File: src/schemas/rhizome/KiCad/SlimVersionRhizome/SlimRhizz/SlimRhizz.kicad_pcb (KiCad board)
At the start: 4 copper layers, 136 x 34.5 mm, 19 parts, among them J1 POWER_IN, J2 WS2812_Tip1, J3 WS2812_Tip2, J4 APA102_Strip, J5 Haptic_DRV1, J6 Haptic_DRV2, J7 Pogo_Male, J8 Pogo_Female, U2 74AHCT125

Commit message: Update PCB
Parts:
- added G***: LOGO, Logo Synapse:logo, B.Cu at (119.5, 124.0)
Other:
- board text added: "+"
- board text added: "-"
- board text added: "Haptic_Femelle"
- board text added: "Haptic_Male"
- board text added: "LED_Embout_Femelle"
- board text added: "LED_Embout_Male"
- board text added: "Power_in"
- board text added: "Serial_Male"

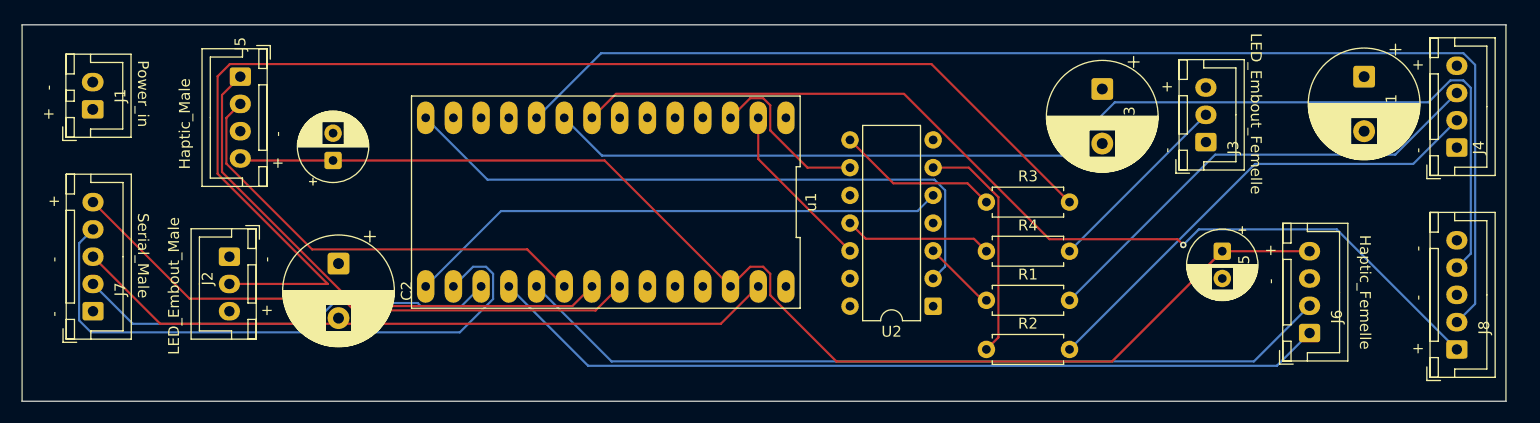
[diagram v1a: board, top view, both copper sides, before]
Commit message: Update PCB SlimRhizz
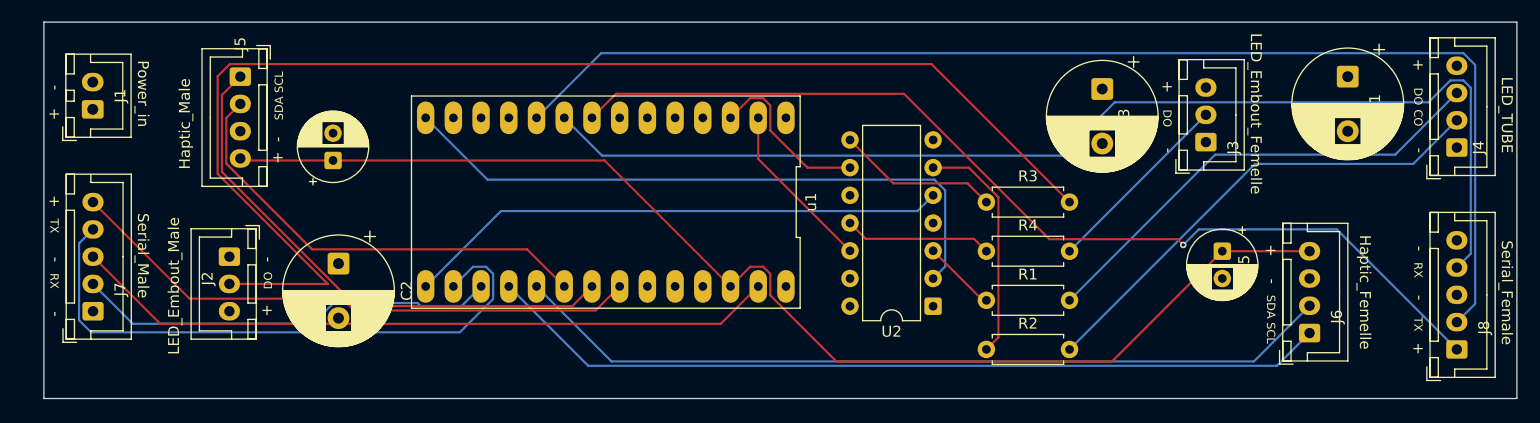
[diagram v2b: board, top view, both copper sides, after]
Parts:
- J4: value APA102_Strip -> LED_TUBE
- moved C1 1.50 mm to (177.0, 112.0)
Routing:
- net GND: track 71.2 -> 71.8 mm
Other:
- board size 136 x 34.5 mm -> 135 x 34.5 mm
- board text added: "CO"
- board text added: "DO"
- board text added: "LED_TUBE"
- board text added: "RX"
- board text added: "SCL"
- board text added: "SDA"
- board text added: "Serial_Female"
- board text added: "TX"
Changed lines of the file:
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@@
 			)
 		)
-		(property "Value" "APA102_Strip"
-			(at 3.75 4.6 90)
+		(property "Value" "LED_TUBE"
+			(at -3.5 -0.5 90)
 			(layer "F.Fab")
+			(hide yes)
 			(effects
 				(font
@@
 	(footprint "Capacitor_THT:CP_Radial_D10.0mm_P5.00mm"
 		(layer "F.Cu")
-		(at 178.5 112 -90)
+		(at 177 112 -90)
 		(descr "CP, Radial series, Radial, pin pitch=5.00mm, diameter=10mm, height=16mm, Electrolytic Capacitor")
 		(tags "CP Radial series Radial pin pitch 5.00mm diameter 10mm height 16mm Electrolytic Capacitor")
@@
 		(tags "CP Radial series Radial pin pitch 5.00mm diameter 10mm height 16mm Electrolytic Capacitor")
 		(property "Reference" "C3"
-			(at 2.5 -2.5 90)
+			(at 2.7 -2.002438 90)
 			(layer "F.SilkS")
 			(effects
@@
 		)
 		(fp_text user "${REFERENCE}"
-			(at 2.5 0 90)
+			(at 2.714285 -2.002438 90)
 			(layer "F.Fab")
 			(effects
@@
 			(at 5 4.6 90)
 			(layer "F.Fab")
+			(hide yes)
 			(effects
 				(font
@@
 			(at 0 0 0)
 			(layer "B.SilkS")
+			(hide yes)
 			(effects
 				(font
@@
 	)
 	(gr_rect
-		(start 55.5 107.25)
-		(end 191.5 141.75)
+		(start 57.5 107)
+		(end 192.5 141.5)
 		(stroke
 			(width 0.05)
@@
 		)
 	)
+	(gr_text "RX"
+		(at 58 130 270)
+		(layer "F.SilkS")
+		(effects
+			(font
+				(size 0.762 0.762)
+				(thickness 0.09525)
+			)
+			(justify left bottom)
+		)
+	)
 	(gr_text "LED_Embout_Male"
 		(at 70 137.5 90)
@@
 		)
 	)
+	(gr_text "SDA"
+		(at 79.5 116 90)
+		(layer "F.SilkS")
+		(effects
+			(font
+				(size 0.762 0.762)
+				(thickness 0.09525)
+			)
+			(justify left bottom)
+		)
+	)
 	(gr_text "Power_in"
 		(at 66 110.5 270)
@@
 	)
 	(gr_text "-"
-		(at 58.5 113.25 90)
+		(at 59 113.25 90)
 		(layer "F.SilkS")
 		(effects
@@
 		)
 	)
+	(gr_text "TX\n"
+		(at 58 125 270)
+		(layer "F.SilkS")
+		(effects
+			(font
+				(size 0.762 0.762)
+				(thickness 0.09525)
+			)
+			(justify left bottom)
+		)
+	)
 	(gr_text "-"
 		(at 184 128 90)
@@
 		)
 	)
+	(gr_text "Serial_Female"
+		(at 191 127 270)
+		(layer "F.SilkS")
+		(effects
+			(font
+				(size 1 1)
+				(thickness 0.1)
+			)
+			(justify left bottom)
+		)
+	)
+	(gr_text "SDA"
+		(at 169.5 132 270)
+		(layer "F.SilkS")
+		(effects
+			(font
+				(size 0.762 0.762)
+				(thickness 0.09525)
+			)
+			(justify left bottom)
+		)
+	)
 	(gr_text "+"
 		(at 161 113.5 90)
@@
 		)
 	)
+	(gr_text "SCL"
+		(at 169.5 134.5 270)
+		(layer "F.SilkS")
+		(effects
+			(font
+				(size 0.762 0.762)
+				(thickness 0.09525)
+			)
+			(justify left bottom)
+		)
+	)
 	(gr_text "+"
 		(at 184 111.5 90)
@@
 		)
 	)
+	(gr_text "DO"
+		(at 78.5 131.5 90)
+		(layer "F.SilkS")
+		(effects
+			(font
+				(size 0.762 0.762)
+				(thickness 0.09525)
+			)
+			(justify left bottom)
+		)
+	)
 	(gr_text "-"
 		(at 161 119 90)
@@
 	)
 	(gr_text "+"
-		(at 79.5 120.5 90)
+		(at 79.5 120 90)
 		(layer "F.SilkS")
 		(effects
@@
 		)
 	)
+	(gr_text "CO"
+		(at 183 115 270)
+		(layer "F.SilkS")
+		(effects
+			(font
+				(size 0.762 0.762)
+				(thickness 0.09525)
+			)
+			(justify left bottom)
+		)
+	)
 	(gr_text "+"
-		(at 58.5 116 90)
+		(at 59 116 90)
 		(layer "F.SilkS")
 		(effects
@@
 		)
 	)
+	(gr_text "DO"
+		(at 160 115 270)
+		(layer "F.SilkS")
+		(effects
+			(font
+				(size 0.762 0.762)
+				(thickness 0.09525)
+			)
+			(justify left bottom)
+		)
+	)
 	(gr_text "-"
 		(at 184 132.5 90)
@@
 		)
 	)
+	(gr_text "RX"
+		(at 183 129 270)
+		(layer "F.SilkS")
+		(effects
+			(font
+				(size 0.762 0.762)
+				(thickness 0.09525)
+			)
+			(justify left bottom)
+		)
+	)
 	(gr_text "+"
 		(at 59 124 90)
@@
 	)
 	(gr_text "-"
-		(at 79.5 117.5 90)
+		(at 79.5 118 90)
 		(layer "F.SilkS")
 		(effects
@@
 		)
 	)
+	(gr_text "LED_TUBE"
+		(at 191 112 270)
+		(layer "F.SilkS")
+		(effects
+			(font
+				(size 1 1)
+				(thickness 0.1)
+			)
+			(justify left bottom)
+		)
+	)
 	(gr_text "Haptic_Male"
 		(at 71 120.5 90)
@@
 		)
 	)
+	(gr_text "SCL"
+		(at 79.5 113.5 90)
+		(layer "F.SilkS")
+		(effects
+			(font
+				(size 0.762 0.762)
+				(thickness 0.09525)
+			)
+			(justify left bottom)
+		)
+	)
 	(gr_text "LED_Embout_Femelle"
 		(at 168 108 270)
@@
 		)
 	)
+	(gr_text "DO"
+		(at 183 113 270)
+		(layer "F.SilkS")
+		(effects
+			(font
+				(size 0.762 0.762)
+				(thickness 0.09525)
+			)
+			(justify left bottom)
+		)
+	)
+	(gr_text "TX\n"
+		(at 183 134 270)
+		(layer "F.SilkS")
+		(effects
+			(font
+				(size 0.762 0.762)
+				(thickness 0.09525)
+			)
+			(justify left bottom)
+		)
+	)
 	(gr_text "-"
 		(at 59 129 90)
@@
 	)
 	(segment
-		(start 177.5 118)
-		(end 178.5 117)
-		(width 0.2)
-		(layer "In1.Cu")
-		(net 34)
-	)
-	(segment
 		(start 131.38 130.5)
 		(end 132.481 129.399)
@@
 	)
 	(segment
+		(start 178.5 118)
+		(end 178.5 117)
+		(width 0.2)
+		(layer "In1.Cu")
+		(net 34)
+	)
+	(segment
 		(start 131.38 130.5)
 		(end 132 130.5)
 		(width 0.2)
 		(layer "In1.Cu")
+		(net 34)
+	)
+	(segment
+		(start 177.5 118)
+		(end 178.5 118)
+		(width 0.2)
+		(layer "In1.Cu")

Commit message: update PCB
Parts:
- moved C4 1.00 mm to (83.0, 119.7)
- moved C1 0.50 mm to (177.5, 112.0)
- moved C2 0.50 mm to (84.0, 129.1)
- moved C5 0.50 mm to (166.0, 128.0)
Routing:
- net +5V: track 425.1 -> 2.82 mm
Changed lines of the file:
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@@
 			(psnegative no)
 			(psa4output no)
-			(plot_black_and_white yes)
+			(plot_black_and_white no)
 			(sketchpadsonfab no)
 			(plotpadnumbers no)
@@
 			(crossoutdnponfab yes)
 			(subtractmaskfromsilk no)
-			(outputformat 1)
+			(outputformat 4)
 			(mirror no)
 			(drillshape 0)
 			(scaleselection 1)
-			(outputdirectory "C:/Users/lepit/Downloads/")
+			(outputdirectory "./")
 		)
 	)
@@
 			(at 0 2 90)
 			(layer "F.SilkS")
+			(hide yes)
 			(effects
 				(font
@@
 	(footprint "Capacitor_THT:CP_Radial_D10.0mm_P5.00mm"
 		(layer "F.Cu")
-		(at 177 112 -90)
+		(at 177.5 112 -90)
 		(descr "CP, Radial series, Radial, pin pitch=5.00mm, diameter=10mm, height=16mm, Electrolytic Capacitor")
 		(tags "CP Radial series Radial pin pitch 5.00mm diameter 10mm height 16mm Electrolytic Capacitor")
 		(property "Reference" "C1"
-			(at 2.5 -2.5 90)
+			(at 2 6 90)
 			(layer "F.SilkS")
 			(effects
@@
 	(footprint "Capacitor_THT:CP_Radial_D6.3mm_P2.50mm"
 		(layer "F.Cu")
-		(at 165.5 128 -90)
+		(at 166 128 -90)
 		(descr "CP, Radial series, Radial, pin pitch=2.50mm, diameter=6.3mm, height=7mm, Electrolytic Capacitor")
 		(tags "CP Radial series Radial pin pitch 2.50mm diameter 6.3mm height 7mm Electrolytic Capacitor")
 		(property "Reference" "C5"
-			(at 1.25 -2 90)
+			(at 1.5 4.5 90)
 			(layer "F.SilkS")
 			(effects
@@
 		(tags "CP Radial series Radial pin pitch 5.00mm diameter 10mm height 16mm Electrolytic Capacitor")
 		(property "Reference" "C3"
-			(at 2.7 -2.002438 90)
+			(at 1.867677 6 90)
 			(layer "F.SilkS")
 			(effects
@@
 			(at 1.5 2.5 90)
 			(layer "F.SilkS")
+			(hide yes)
 			(effects
 				(font
@@
 			(at 2 2.5 90)
 			(layer "F.SilkS")
+			(hide yes)
 			(effects
 				(font
@@
 		(tags "connector JST XH vertical")
 		(property "Reference" "J3"
-			(at -0.5 2.5 90)
+			(at -5 -0.5 90)
 			(layer "F.SilkS")
+			(hide yes)
 			(effects
 				(font
@@
 	(footprint "Capacitor_THT:CP_Radial_D10.0mm_P5.00mm"
 		(layer "F.Cu")
-		(at 84.5 129.132323 -90)
+		(at 84 129.132323 -90)
 		(descr "CP, Radial series, Radial, pin pitch=5.00mm, diameter=10mm, height=16mm, Electrolytic Capacitor")
 		(tags "CP Radial series Radial pin pitch 5.00mm diameter 10mm height 16mm Electrolytic Capacitor")
 		(property "Reference" "C2"
-			(at 2.5 -6.25 90)
+			(at 2.5 -6 90)
 			(layer "F.SilkS")
 			(effects
@@
 			(at 2 2 90)
 			(layer "F.SilkS")
+			(hide yes)
 			(effects
 				(font
@@
 			(at 1.25 2.525 90)
 			(layer "F.SilkS")
+			(hide yes)
 			(effects
 				(font
@@
 			(at -3 0 90)
 			(layer "F.SilkS")
+			(hide yes)
 			(effects
 				(font
@@
 			(at 2 2.5 90)
 			(layer "F.SilkS")
+			(hide yes)
 			(effects
 				(font
@@
 	(footprint "Capacitor_THT:CP_Radial_D6.3mm_P2.50mm"
 		(layer "F.Cu")
-		(at 84 119.68238 90)
+		(at 83 119.68238 90)
 		(descr "CP, Radial series, Radial, pin pitch=2.50mm, diameter=6.3mm, height=7mm, Electrolytic Capacitor")
 		(tags "CP Radial series Radial pin pitch 2.50mm diameter 6.3mm height 7mm Electrolytic Capacitor")
 		(property "Reference" "C4"
-			(at 2.73 1.958 90)
+			(at 1.18238 4.5 90)
 			(layer "F.SilkS")
 			(effects
@@
 	)
 	(segment
-		(start 80 133.5)
-		(end 74.5 133.5)
-		(width 0.2)
-		(layer "In2.Cu")
-		(net 33)
-	)
-	(segment
-		(start 186 112)
-		(end 187 111)
-		(width 0.2)
-		(layer "In2.Cu")
-		(net 33)
-	)
-	(segment
 		(start 61.975 115)
 		(end 62 115)
@@
 	)
 	(segment
-		(start 90.356951 115.651)
-		(end 94.007951 112)
-		(width 0.2)
-		(layer "In2.Cu")
-		(net 33)
-	)
-	(segment
-		(start 127.739 129.399)
-		(end 131.38 133.04)
-		(width 0.2)
-		(layer "In2.Cu")
-		(net 33)
-	)
-	(segment
-		(start 84.367677 129.132323)
-		(end 80 133.5)
-		(width 0.2)
-		(layer "In2.Cu")
-		(net 33)
-	)
-	(segment
-		(start 155 113)
-		(end 164 113)
-		(width 0.2)
-		(layer "In2.Cu")
-		(net 33)
-	)
-	(segment
-		(start 63.16116 115)
-		(end 77.56016 129.399)
-		(width 0.2)
-		(layer "In2.Cu")
-		(net 33)
-	)
-	(segment
-		(start 178.5 112)
-		(end 186 112)
-		(width 0.2)
-		(layer "In2.Cu")
-		(net 33)
-	)
-	(segment
-		(start 91.85546 129.424)
-		(end 123.709 129.424)
-		(width 0.2)
-		(layer "In2.Cu")
-		(net 33)
-	)
-	(segment
-		(start 61.975 115)
-		(end 67.626 120.651)
-		(width 0.2)
-		(layer "In2.Cu")
-		(net 33)
-	)
-	(segment
-		(start 71.294 124.319)
-		(end 141.50395 124.319)
-		(width 0.2)
-		(layer "In2.Cu")
-		(net 33)
-	)
-	(segment
 		(start 84.5 129.132323)
 		(end 84.367677 129.132323)
@@
 	)
 	(segment
-		(start 62.626 115.651)
-		(end 90.356951 115.651)
-		(width 0.2)
-		(layer "In2.Cu")
-		(net 33)
-	)
-	(segment
 		(start 61.975 115)
 		(end 62.626 115.651)
@@
 	)
 	(segment
-		(start 123.709 129.424)
-		(end 125.51 131.225)
-		(width 0.2)
-		(layer "In2.Cu")
-		(net 33)
-	)
-	(segment
 		(start 61.975 115)
 		(end 63.16116 115)
@@
 	)
 	(segment
-		(start 67.651 120.651)
-		(end 83.08246 120.651)
-		(width 0.2)
-		(layer "In2.Cu")
-		(net 33)
-	)
-	(segment
 		(start 154.867677 113.132323)
 		(end 155 113)
 		(width 0.2)
 		(layer "In2.Cu")
-		(net 33)
-	)
-	(segment
-		(start 62 115)
-		(end 67.651 120.651)
-		(width 0.2)
-		(layer "In2.Cu")
-		(net 33)
-	)
-	(segment
-		(start 152.690627 113.132323)
-		(end 154.5 113.132323)
-		(width 0.2)
-		(layer "In2.Cu")
-		(net 33)
-	)
-	(segment
-		(start 77.56016 129.399)
-		(end 127.739 129.399)
-		(width 0.2)
-		(layer "In2.Cu")
-		(net 33)
-	)
-	(segment
-		(start 94.007951 112)
-		(end 178.5 112)
-		(width 0.2)
-		(layer "In2.Cu")
-		(net 33)
-	)
-	(segment
-		(start 67.626 120.651)
-		(end 76.018677 120.651)
-		(width 0.2)
-		(layer "In2.Cu")
-		(net 33)
-	)
-	(segment
-		(start 61.975 115)
-		(end 71.294 124.319)
-		(width 0.2)
-		(layer "In2.Cu")
-		(net 33)
-	)
-	(segment
-		(start 83.08246 120.651)
-		(end 91.85546 129.424)
-		(width 0.2)
-		(layer "In2.Cu")
-		(net 33)
-	)
-	(segment
-		(start 141.50395 124.319)
-		(end 152.690627 113.132323)
-		(width 0.2)
-		(layer "In2.Cu")
-		(net 33)
-	)
-	(segment
-		(start 76.018677 120.651)
-		(end 84.5 129.132323)
-		(width 0.2)
-		(layer "In2.Cu")

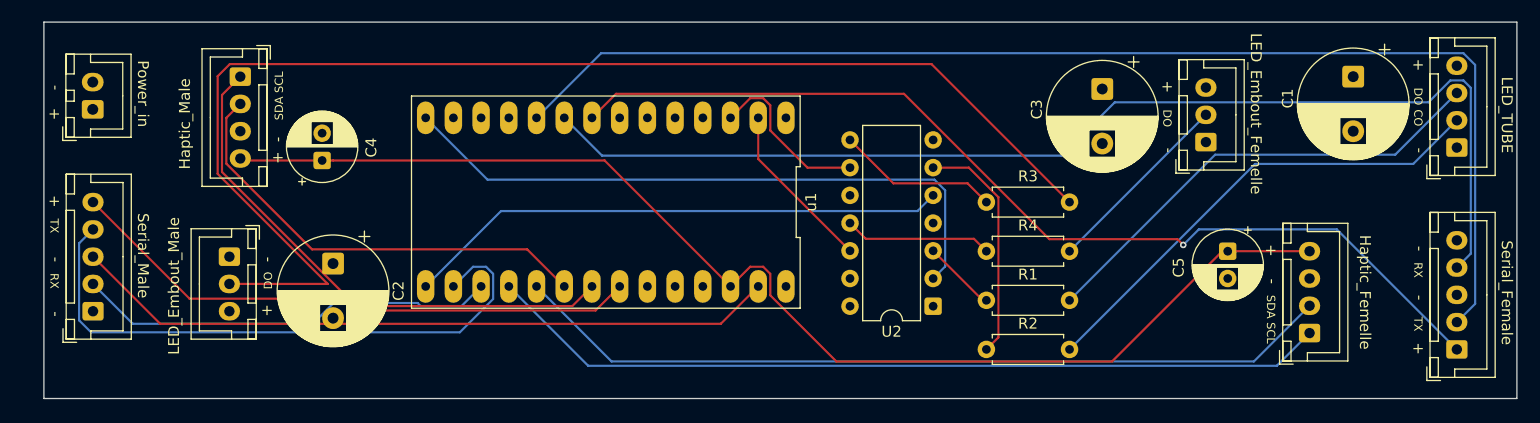
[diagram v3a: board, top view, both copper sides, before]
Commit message: PCB Trace Width Fix
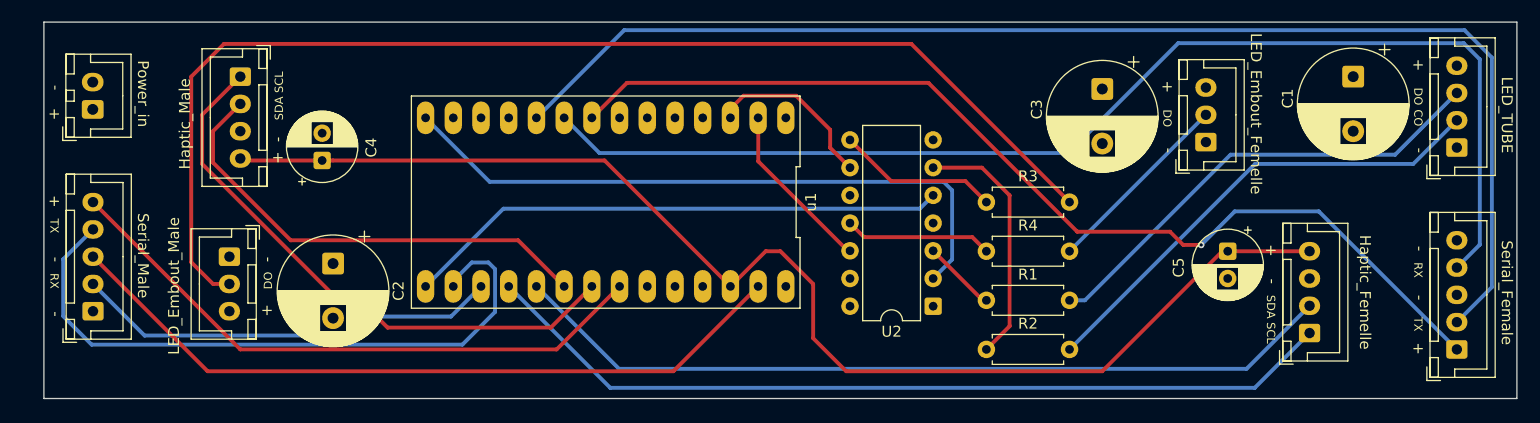
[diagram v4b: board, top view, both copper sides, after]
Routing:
- net Net-(J2-Pin_2): track 116.0 -> 109.1 mm
- net Net-(J8-Pin_4): track 104.7 -> 110.0 mm
- net Net-(J7-Pin_4): track 55.5 -> 60.2 mm
- net Net-(J8-Pin_2): track 113.2 -> 117.5 mm
- net Net-(J5-Pin_1): track 49.2 -> 53.0 mm
- net Net-(J5-Pin_4): track 112.5 -> 116.2 mm
- net GND: track 71.8 -> 75.4 mm
- net Net-(J7-Pin_5): track 53.3 -> 56.3 mm
- net Net-(J8-Pin_1): track 91.1 -> 93.3 mm
- net Net-(J5-Pin_2): track 41.6 -> 43.3 mm
- net Net-(J6-Pin_1): track 77.6 -> 79.3 mm
- net Net-(R2-Pad1): track 21.5 -> 23.1 mm
- net /APA_CLK_PRE: track 58.9 -> 59.8 mm
- net Net-(J7-Pin_2): track 38.7 -> 39.4 mm
- net Net-(J6-Pin_2): track 75.8 -> 76.4 mm

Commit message: pcb v2
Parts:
- added D1: PWR, LED_SMD:LED_0402_1005Metric, F.Cu at (71.2, 113.2)
- added HBT: HBT, LED_SMD:LED_0402_1005Metric, F.Cu at (118.8, 113.8)
- added LCon: L-Connect, LED_SMD:LED_0402_1005Metric, F.Cu at (115.5, 113.8)
- added PWR: 1000, Resistor_SMD:R_0402_1005Metric, F.Cu at (71.2, 114.5)
- added R6: 330, Resistor_SMD:R_0402_1005Metric, F.Cu at (118.8, 114.8)
- added R7: 330, Resistor_SMD:R_0402_1005Metric, F.Cu at (115.5, 114.8)
- added R8: 330, Resistor_SMD:R_0402_1005Metric, F.Cu at (112.0, 114.8)
- added RCon: R-Connect, LED_SMD:LED_0402_1005Metric, F.Cu at (112.0, 113.8)
- C1, C2, C3: footprint Capacitor_THT:CP_Radial_D10.0mm_P5.00mm -> Capacitor_SMD:CP_Elec_10x10.5
- C4, C5: footprint Capacitor_THT:CP_Radial_D6.3mm_P2.50mm -> Capacitor_SMD:CP_Elec_6.3x5.4
- J4: value LED_TUBE -> APA102_Strip
- R1, R2, R4: footprint Resistor_THT:R_Axial_DIN0207_L6.3mm_D2.5mm_P7.62mm_Horizontal -> Resistor_SMD:R_0805_2012Metric
- R3: value 330 -> 220; footprint Resistor_THT:R_Axial_DIN0207_L6.3mm_D2.5mm_P7.62mm_Horizontal -> Resistor_SMD:R_0805_2012Metric
- moved C1 33.2 mm to (149.0, 129.0), turned to 0 degrees
- moved J4 31.6 mm to (159.2, 133.5)
- moved R3 20.6 mm to (125.6, 114.0), turned to 180 degrees
- moved J6 13.2 mm to (177.0, 122.8)
- moved J8 11.0 mm to (177.8, 131.0), turned to 180 degrees
- moved C5 9.84 mm to (168.8, 118.5)
- moved G*** 9.69 mm to (109.9, 125.1)
- moved R1 7.47 mm to (140.2, 126.0)
- moved R2 7.47 mm to (140.2, 130.5)
- moved R4 7.47 mm to (140.2, 121.5)
- moved C3 7.44 mm to (148.4, 117.4), turned to 0 degrees
- moved J3 5.53 mm to (158.8, 119.8)
- moved J1 3.97 mm to (65.2, 117.2)
- moved J7 3.26 mm to (65.2, 133.8)
- moved J5 3.17 mm to (76.5, 115.0)
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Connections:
- u1 pad 2: unconnected-(u1-Pad2) -> Net-(R6-Pad1)
- u1 pad 3: unconnected-(u1-Pad3) -> Net-(R7-Pad1)
- u1 pad 4: unconnected-(u1-Pad4) -> Net-(R8-Pad1)
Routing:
- net +5V: track 2.82 -> 35.9 mm, vias 0 -> 4
- net Net-(J2-Pin_2): track 109.1 -> 77.6 mm, vias 0 -> 2
- net GND: track 75.4 -> 48.4 mm, vias 0 -> 7
- net Net-(J4-Pin_2): track 44.2 -> 19.0 mm, vias 0 -> 2
- net Net-(J7-Pin_4): track 60.2 -> 36.8 mm
- net Net-(J8-Pin_2): track 117.5 -> 97.7 mm, vias 0 -> 1
- net Net-(J4-Pin_3): track 43.4 -> 24.3 mm
- net Net-(J8-Pin_4): track 110.0 -> 96.3 mm
- net /APA_CLK_PRE: track 59.8 -> 48.3 mm
- net Net-(R3-Pad1): track 14.9 -> 3.45 mm
- net Net-(J5-Pin_1): track 53.0 -> 42.3 mm
- net Net-(R2-Pad1): track 23.1 -> 14.6 mm, vias 0 -> 1
- net Net-(J5-Pin_2): track 43.3 -> 35.7 mm
- net Net-(J5-Pin_4): track 116.2 -> 122.6 mm
- net /LED_TIP1: track 16.0 -> 10.1 mm
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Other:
- board size 135 x 34.5 mm -> 122.2 x 26.5 mm
- board text added: "Big shoutout à la Cohorte de feu"
- board text added: "Haptic_F"
- board text added: "Haptic_M"
- board text added: "LED_EmboutF"
- board text added: "LED_EmboutM"
- board text added: "Mery on va dehors"
- board text added: "PCB DESIGN: Clément Boucher Justin Lepitre"
- board text added: "Raton was there"
- board text added: "Serial_F"
- board text added: "Serial_M"
- board text added: "Sorry Jc ya pu de son :("
- board text added: "Version 2.0"
- board text removed: "Haptic_Femelle"
- board text removed: "Haptic_Male"
- board text removed: "LED_Embout_Femelle"
- board text removed: "LED_Embout_Male"
- board text removed: "Serial_Female"
- board text removed: "Serial_Male"
